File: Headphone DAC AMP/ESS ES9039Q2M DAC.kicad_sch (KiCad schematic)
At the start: 5 parts

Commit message: Updating Changes
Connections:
- net NODE renamed MODE
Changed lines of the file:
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@@
 		)
 	)
-	(hierarchical_label "NODE"
+	(hierarchical_label "MODE"
 		(shape output)
 		(at 106.68 100.33 180)

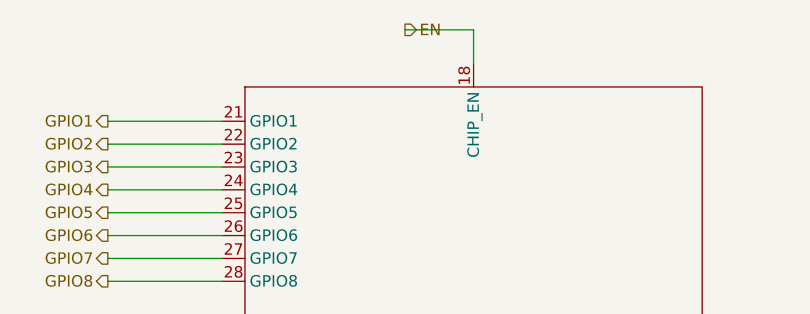
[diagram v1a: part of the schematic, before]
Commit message: Began connecting Root page
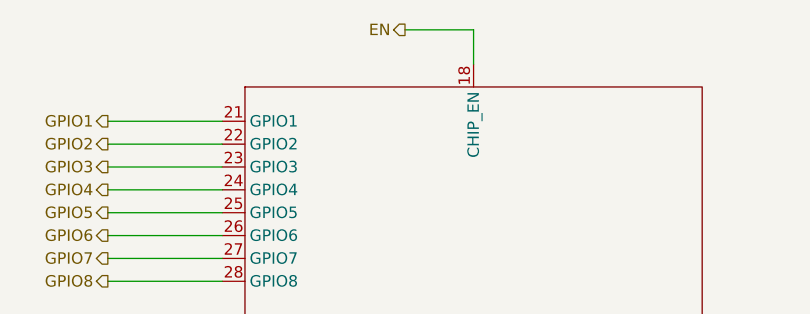
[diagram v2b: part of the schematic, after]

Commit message: Completed a significant amount of the power and routing
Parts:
- C1, C2, C3, C4: footprint (none) -> Capacitor_SMD:C_0805_2012Metric_Pad1.18x1.45mm_HandSolder
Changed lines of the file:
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@@
 			)
 		)
-		(property "Footprint" ""
+		(property "Footprint" "Capacitor_SMD:C_0805_2012Metric_Pad1.18x1.45mm_HandSolder"
 			(at 194.0052 123.19 0)
 			(effects
@@
 			)
 		)
-		(property "Footprint" ""
+		(property "Footprint" "Capacitor_SMD:C_0805_2012Metric_Pad1.18x1.45mm_HandSolder"
 			(at 207.9752 123.19 0)
 			(effects
@@
 			)
 		)
-		(property "Footprint" ""
+		(property "Footprint" "Capacitor_SMD:C_0805_2012Metric_Pad1.18x1.45mm_HandSolder"
 			(at 109.22 132.3848 0)
 			(effects
@@
 			)
 		)
-		(property "Footprint" ""
+		(property "Footprint" "Capacitor_SMD:C_0805_2012Metric_Pad1.18x1.45mm_HandSolder"
 			(at 115.57 129.8448 0)
 			(effects

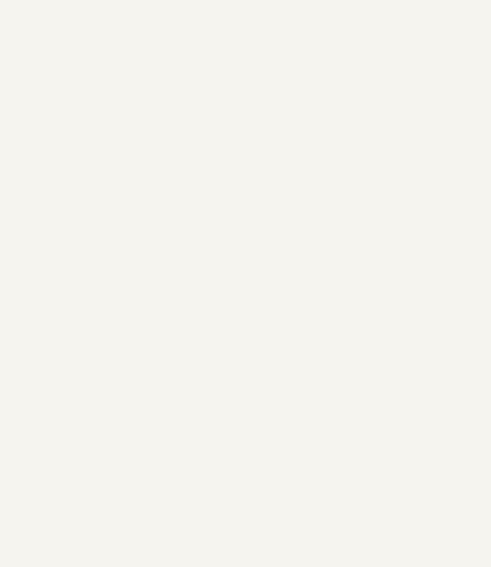
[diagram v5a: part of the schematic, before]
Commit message: Added ground and 0.9v
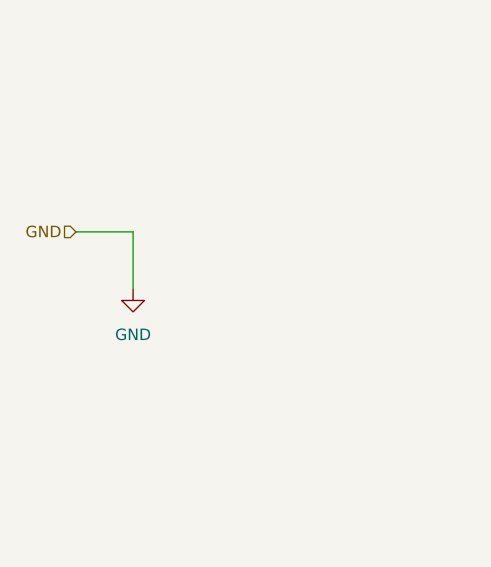
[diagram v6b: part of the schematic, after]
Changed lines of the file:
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@@
 	(wire
 		(pts
+			(xy 52.07 118.11) (xy 52.07 124.46)
+		)
+		(stroke
+			(width 0)
+			(type default)
+		)
+	)
+	(wire
+		(pts
 			(xy 107.95 130.81) (xy 97.79 130.81)
 		)
@@
 	(wire
 		(pts
+			(xy 45.72 118.11) (xy 52.07 118.11)
+		)
+		(stroke
+			(width 0)
+			(type default)
+		)
+	)
+	(wire
+		(pts
 			(xy 173.99 104.14) (xy 176.53 104.14)
 		)
@@
 		)
 	)
+	(hierarchical_label "GND"
+		(shape input)
+		(at 45.72 118.11 180)
+		(effects
+			(font
+				(size 1.27 1.27)
+			)
+			(justify right)
+		)
+	)
 	(hierarchical_label "GPIO2"
 		(shape output)
@@
 					(unit 1)
 				)
+			)
+		)
+	)
+	(symbol
+		(lib_id "power:GND")
+		(at 52.07 124.46 0)
+		(unit 1)
+		(exclude_from_sim no)
+		(in_bom yes)
+		(on_board yes)
+		(dnp no)
+		(fields_autoplaced yes)
+		(property "Reference" "#PWR082"
+			(at 52.07 130.81 0)
+			(effects
+				(font
+					(size 1.27 1.27)
+				)
+				(hide yes)
+			)
+		)
+		(property "Value" "GND"
+			(at 52.07 129.54 0)
+			(effects
+				(font
+					(size 1.27 1.27)
+				)
+			)
+		)
+		(property "Footprint" ""
+			(at 52.07 124.46 0)
+			(effects
+				(font
+					(size 1.27 1.27)
+				)
+				(hide yes)
+			)
+		)
+		(property "Datasheet" ""
+			(at 52.07 124.46 0)
+			(effects
+				(font
+					(size 1.27 1.27)
+				)
+				(hide yes)
+			)
+		)
+		(property "Description" "Power symbol creates a global label with name \"GND\" , ground"
+			(at 52.07 124.46 0)
+			(effects
+				(font
+					(size 1.27 1.27)
+				)
+				(hide yes)
+			)
+		)
+		(pin "1"
+		)
+		(instances
+			(project "Headphone DAC AMP"
+				(path "/d034eddd-efbc-47be-a25c-37cbfbab4cd8/b3fc2b7c-ef32-4c23-9b31-7b4a799376ea"
+					(reference "#PWR082")
+					(unit 1)
+				)

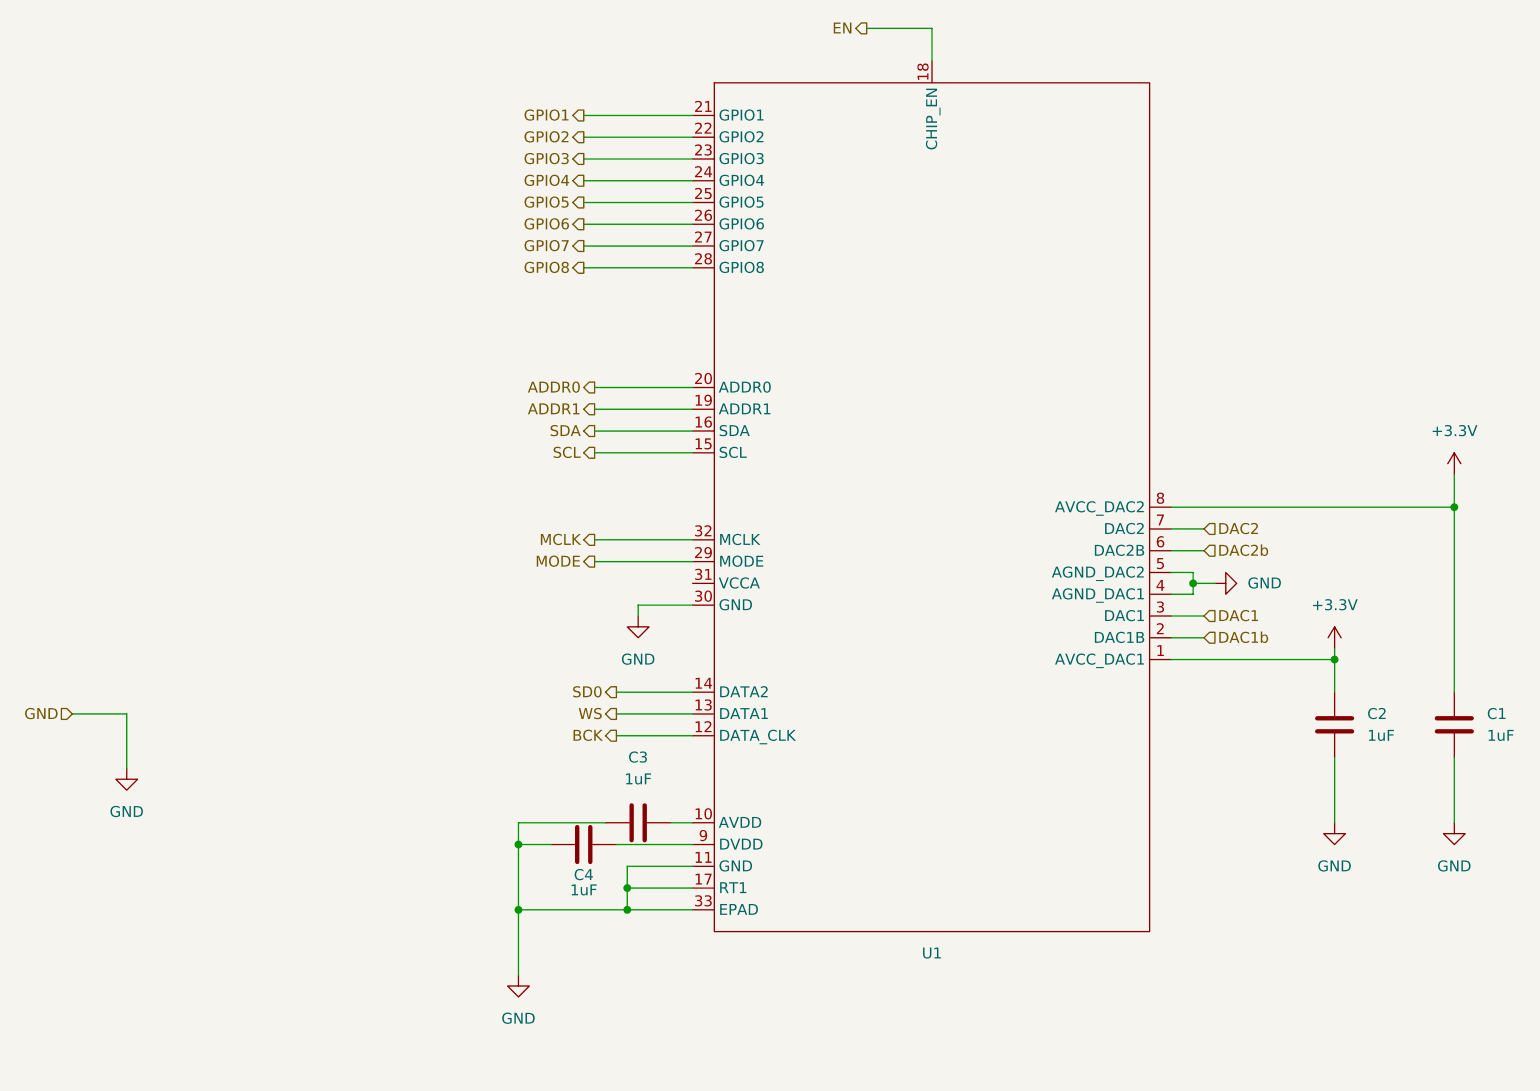
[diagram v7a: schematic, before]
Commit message: Polished DAC GPIOs and connected to XMOS
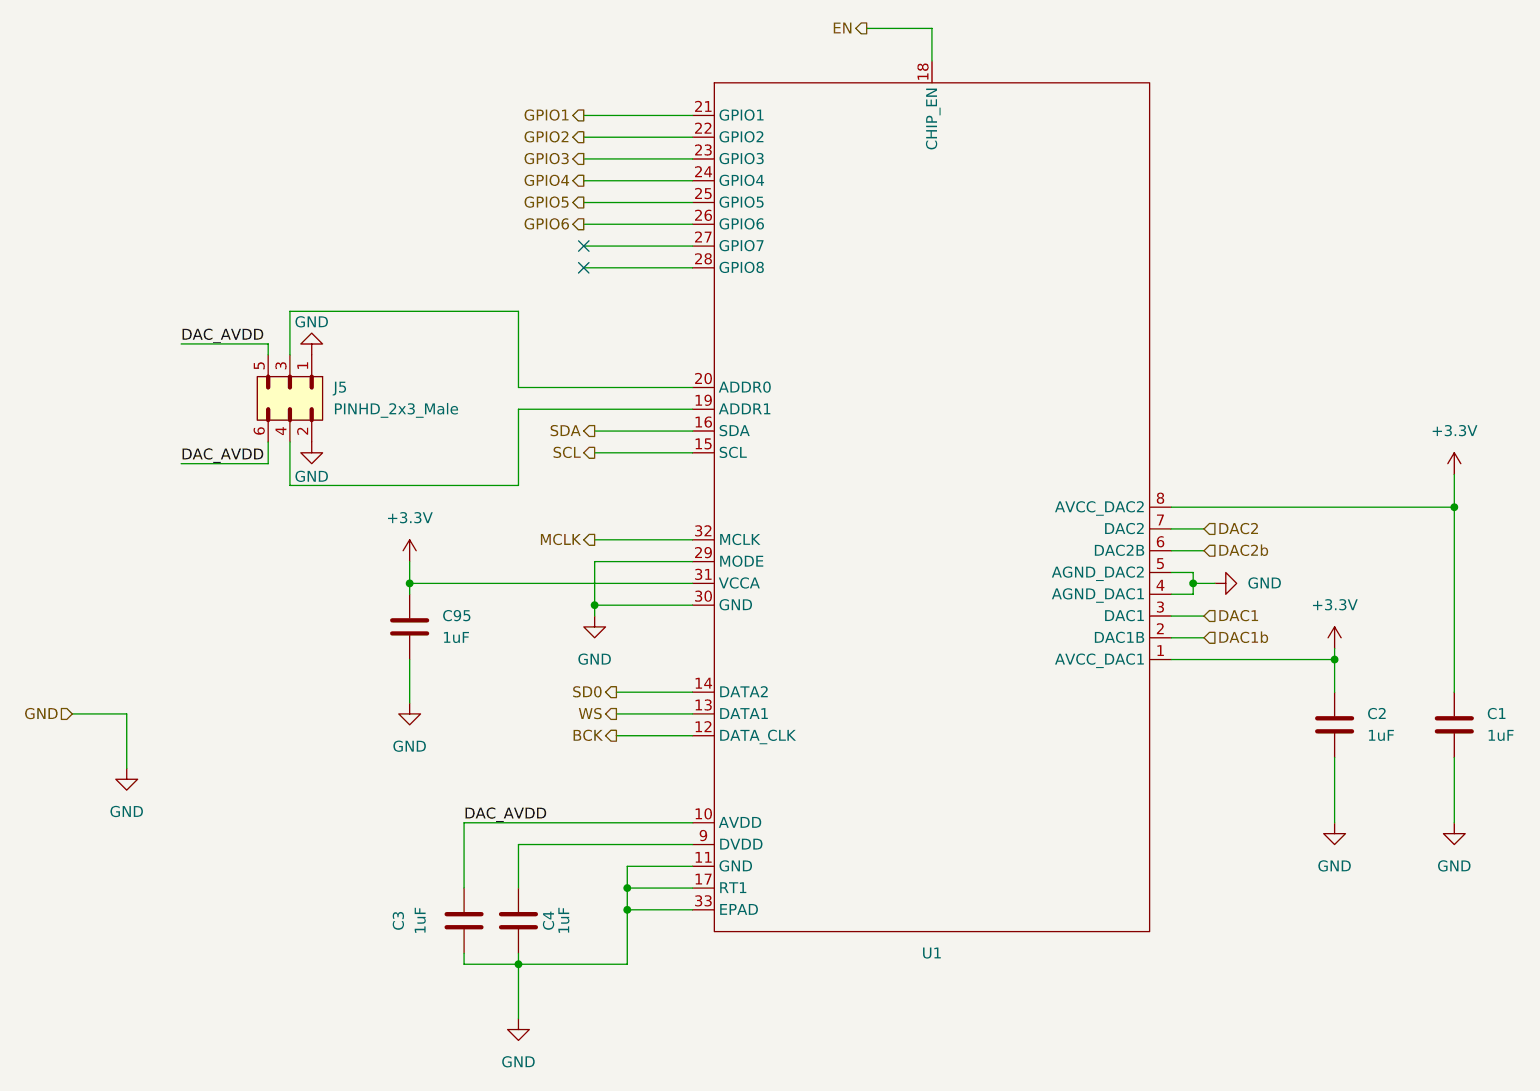
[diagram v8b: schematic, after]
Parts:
- added C95: 1uF, Capacitor_SMD:C_0805_2012Metric_Pad1.18x1.45mm_HandSolder, symbol Device:C
- added J5: PINHD_2x3_Male, Connector_PinHeader_2.54mm:PinHeader_2x03_P2.54mm_Vertical, symbol PCM_SL_Pin_Headers:PINHD_2x3_Male
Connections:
- net MODE is gone; now on net GND: U1.29 (MODE)
- net +3.3V: now also U1.31 (VCCA), C95.1
- net GND: now also C95.2, J5.1, J5.2
- net DAC_AVDD: now reaches C3.2, U1.10 (AVDD)
- net DAC_AVDD: now also J5.5, J5.6
- net ADDR0: no longer names the net of U1.20 (ADDR0)
- net ADDR0: now also J5.3
- net ADDR1: no longer names the net of U1.19 (ADDR1)
- net ADDR1: now also J5.4
- net GPIO7: no longer names the net of U1.27 (GPIO7)
- net GPIO8: no longer names the net of U1.28 (GPIO8)
- no-connect marks 0 -> 2
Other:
- moved on the sheet: C3, C4
